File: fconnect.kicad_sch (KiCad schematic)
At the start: 198 parts, among them J1 9001-11961C00A, J2 9001-11961C00A, J3 7760, J4 7760

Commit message: First try to fit electronic on PCB
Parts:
- TP17, TP18, TP19, TP20, TP21, TP22: footprint Connector_Pin:Pin_D1.2mm_L11.3mm_W3.0mm_Flat -> Connector_Pin:Pin_D1.0mm_L10.0mm
- TP23: renamed from TP25; footprint Connector_Pin:Pin_D1.2mm_L11.3mm_W3.0mm_Flat -> Connector_Pin:Pin_D1.0mm_L10.0mm
- TP24: renamed from TP27; footprint Connector_Pin:Pin_D1.2mm_L11.3mm_W3.0mm_Flat -> Connector_Pin:Pin_D1.0mm_L10.0mm
- TP25: renamed from TP28; footprint Connector_Pin:Pin_D1.2mm_L11.3mm_W3.0mm_Flat -> Connector_Pin:Pin_D1.0mm_L10.0mm
- renumbered NT578 to NT136, NT136 to NT137, NT137 to NT138, NT138 to NT139, NT139 to NT140, NT140 to NT141, NT141 to NT142, NT142 to NT143, NT143 to NT144, NT144 to NT145, NT145 to NT146, NT146 to NT147, NT147 to NT148, NT148 to NT149, NT149 to NT150, NT150 to NT151, NT151 to NT152, NT152 to NT153, NT153 to NT154, NT154 to NT155, NT155 to NT156, NT156 to NT157, NT157 to NT158, NT158 to NT159, NT159 to NT160, NT160 to NT161, NT161 to NT162, NT162 to NT163, NT163 to NT164, NT164 to NT165, NT165 to NT166, NT579 to NT167, NT166 to NT168, NT167 to NT169, NT168 to NT170, NT169 to NT171, NT170 to NT172, NT171 to NT173, NT172 to NT174, NT173 to NT175, NT174 to NT176, NT175 to NT177, NT176 to NT178, NT177 to NT179, NT178 to NT180, NT179 to NT181, NT180 to NT182, NT181 to NT183, NT182 to NT184, NT183 to NT185, NT184 to NT186, NT185 to NT187, NT186 to NT188, NT187 to NT189, NT188 to NT190, NT189 to NT191, NT190 to NT192, NT191 to NT193, NT192 to NT194, NT193 to NT195, NT194 to NT196, NT195 to NT197, NT580 to NT198, NT196 to NT199, NT197 to NT200, NT198 to NT201, NT199 to NT202, NT200 to NT203, NT201 to NT204, NT202 to NT205, NT203 to NT206, NT204 to NT207, NT205 to NT208, NT206 to NT209, NT207 to NT210, NT208 to NT211, NT209 to NT212, NT210 to NT213, NT211 to NT214, NT212 to NT215, NT213 to NT216, NT214 to NT217, NT215 to NT218, NT216 to NT219, NT217 to NT220, NT218 to NT221, NT219 to NT222, NT220 to NT223, NT221 to NT224, NT222 to NT225, NT223 to NT226, NT224 to NT227, NT225 to NT228, NT226 to NT229, NT227 to NT230, NT228 to NT231, NT229 to NT232
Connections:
- net PM3_IO28 renamed PM2_IO28
- net PM3_IO8 renamed PM2_IO8
- net PM3_IO9 renamed PM2_IO9

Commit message: backup 1 bank done
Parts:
- NT100, NT101, NT102, NT103, NT104, NT105, NT106, NT107, NT108, NT109, NT110, NT111, NT112, NT113, NT114, NT115, NT116, NT117, NT118, NT119, NT120, NT121, NT122, NT123, NT124, NT125, NT126, NT127, NT128, NT129, NT130, NT131, NT132, NT133, NT134, NT135, NT136, NT137, NT138, NT139, NT140, NT141, NT142, NT143, NT144, NT145, NT146, NT147, NT148, NT149, NT150, NT151, NT152, NT153, NT154, NT155, NT156, NT157, NT158, NT159, NT160, NT161, NT162, NT163, NT164, NT165, NT166, NT167, NT168, NT169, NT170, NT171, NT172, NT173, NT174, NT175, NT176, NT177, NT178, NT179, NT180, NT181, NT182, NT183, NT184, NT185, NT186, NT187, NT188, NT189, NT190, NT191, NT192, NT193, NT194, NT195, NT196, NT197, NT198, NT199, NT200, NT201, NT202, NT203, NT204, NT205, NT206, NT207, NT208, NT209, NT210, NT211, NT212, NT213, NT214, NT215, NT216, NT217, NT218, NT219, NT220, NT221, NT222, NT223, NT224, NT225, NT226, NT227, NT228, NT229, NT230, NT231, NT232, NT48, NT49, NT50, NT51, NT52, NT53, NT54, NT55, NT56, NT57, NT58, NT59, NT60, NT61, NT62, NT63, NT64, NT65, NT66, NT67, NT68, NT69, NT70, NT71, NT72, NT73, NT74, NT75, NT76, NT77, NT78, NT79, NT80, NT81, NT82, NT83, NT84, NT85, NT86, NT87, NT88, NT89, NT90, NT91, NT92, NT93, NT94, NT95, NT96, NT97, NT98, NT99: footprint NetTie:NetTie-2_THT_Pad1.0mm -> NetTie:NetTie-2_Front1.0mm
- TP17, TP18, TP19, TP20, TP21, TP22, TP23, TP24, TP25: footprint Connector_Pin:Pin_D1.0mm_L10.0mm -> Connector_Pin:Pin_D0.9mm_L10.0mm_W2.4mm_FlatFork
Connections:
- net AWG_H: now also NT135.2; no longer NT135.1
- net AWG_L: now also NT139.2; no longer NT139.1
- net SCOPE_CH1_H: now also NT73.2; no longer NT73.1
- net SCOPE_CH1_L: now also NT76.2; no longer NT76.1
- net at J2.A7: now also NT73.1; no longer NT73.2
- net at J2.A24: now also NT139.1; no longer NT139.2
- net at J2.A23: now also NT135.1; no longer NT135.2
- net at J2.A8: now also NT76.1; no longer NT76.2

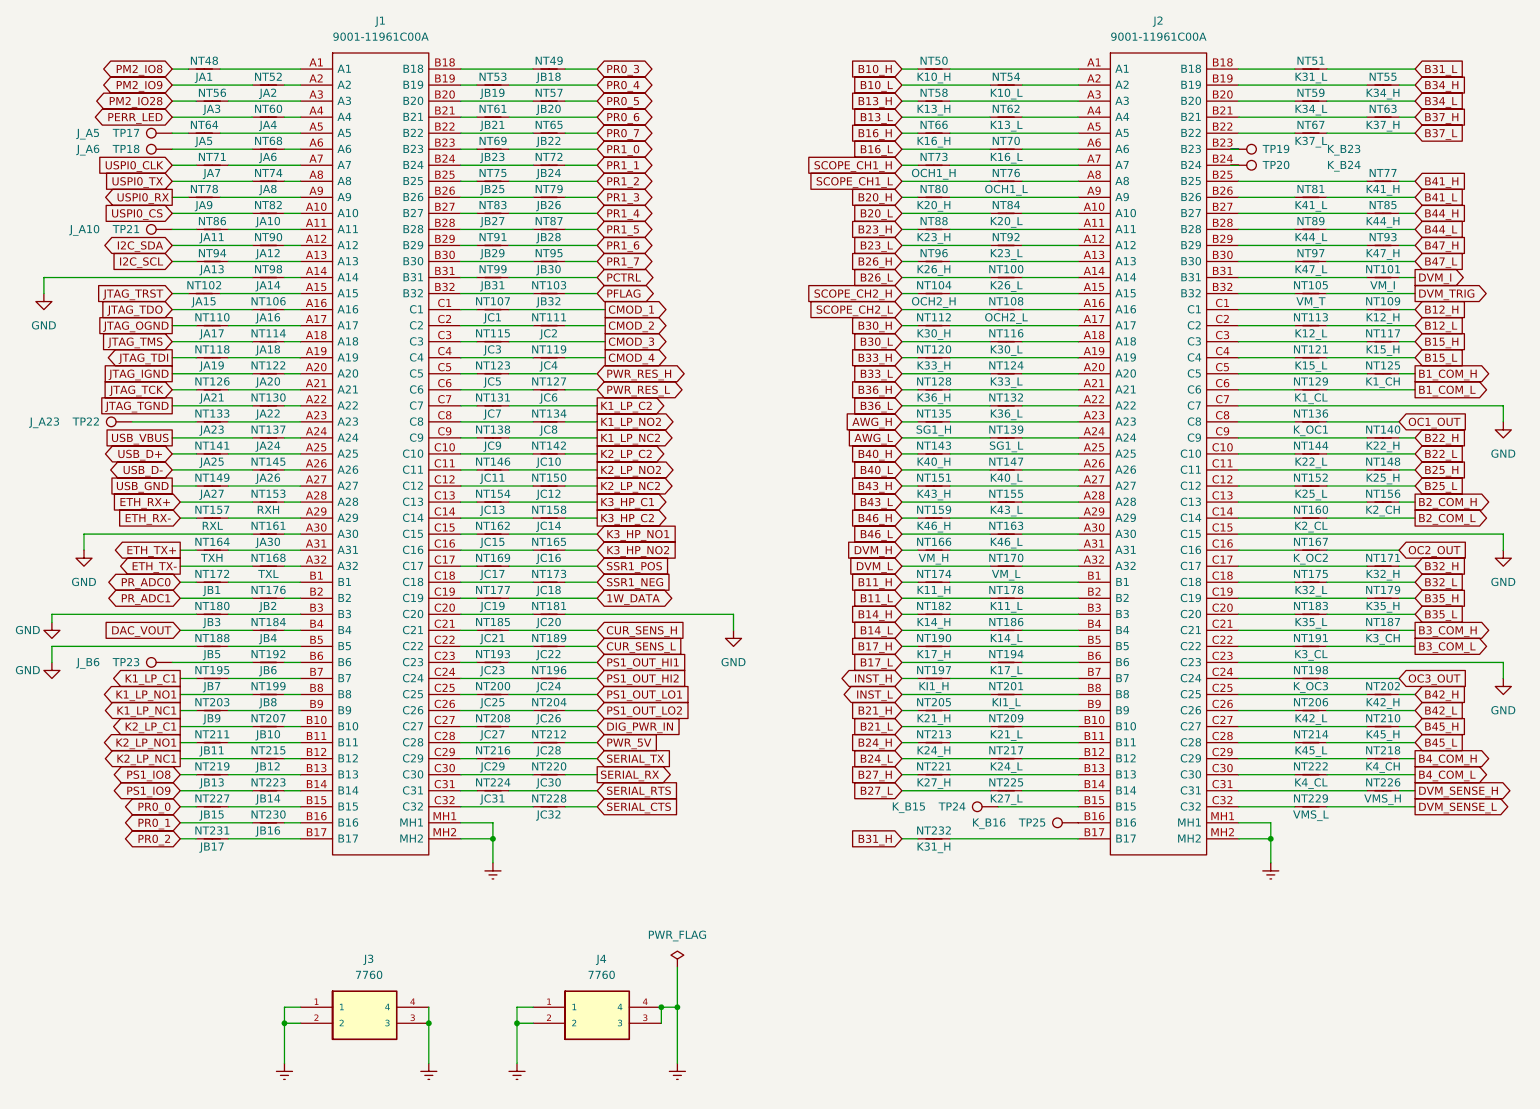
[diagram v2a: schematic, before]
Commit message: half PCB completed
FTS io controller PCB
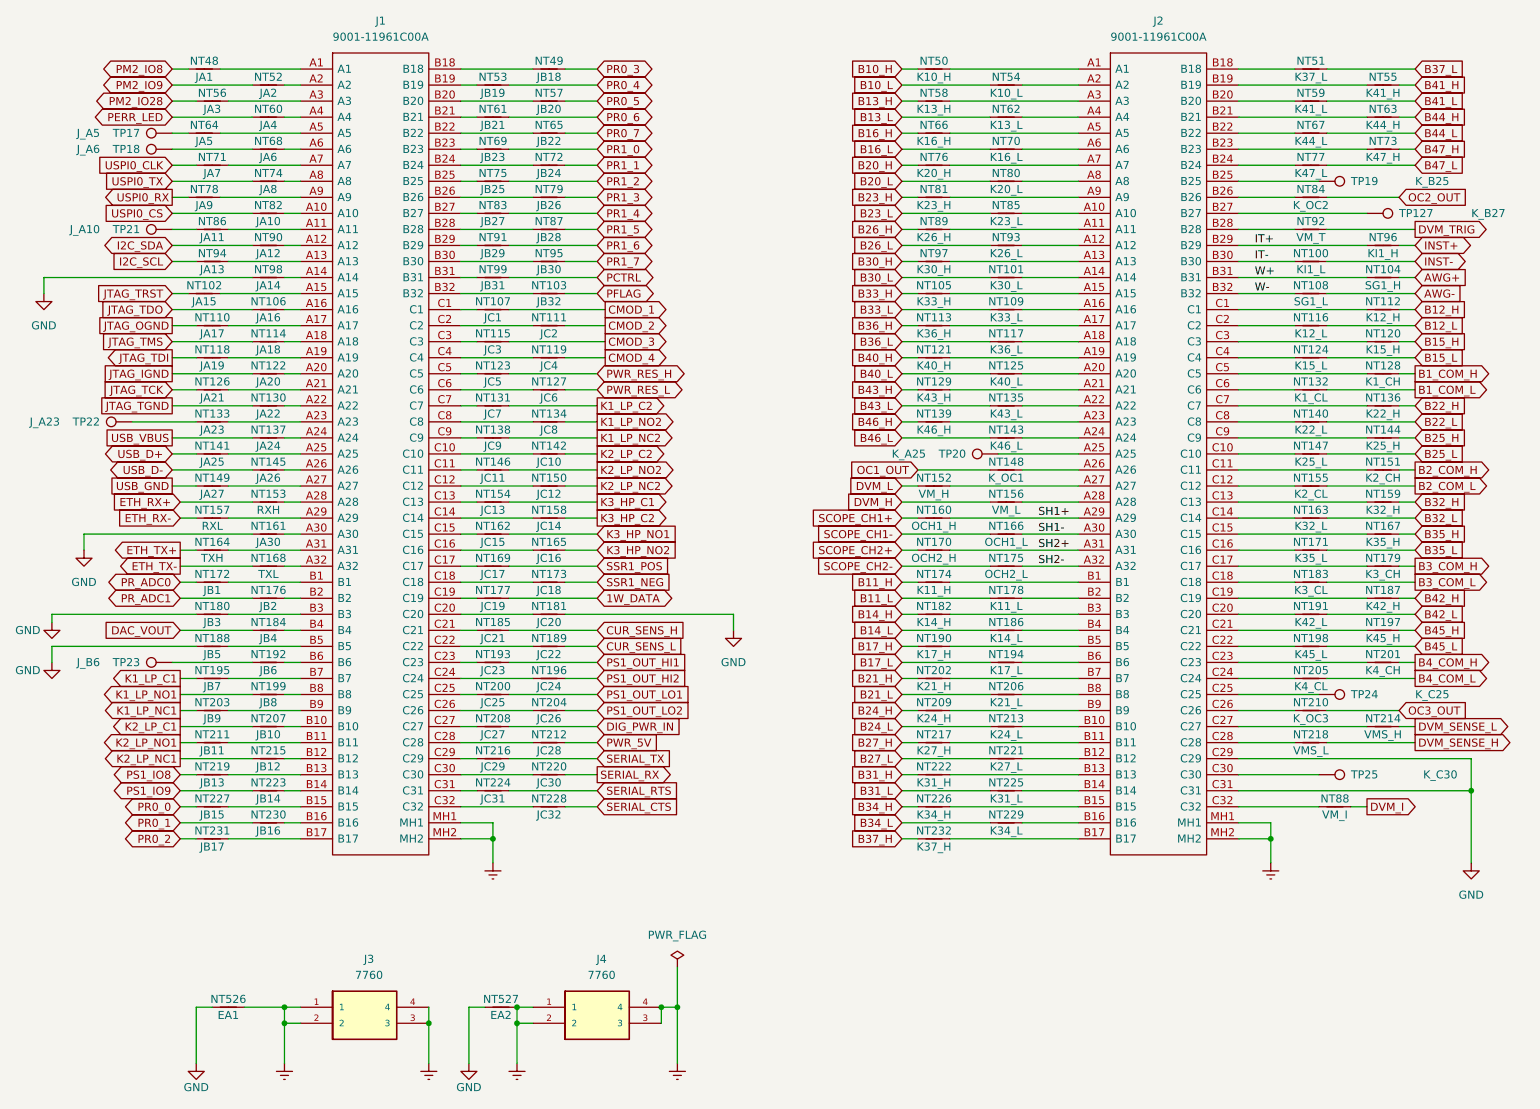
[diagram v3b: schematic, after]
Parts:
- added NT526: EA1, NetTie:NetTie-2_Front1.0mm, symbol Device:NetTie_2
- added NT527: EA2, NetTie:NetTie-2_Front1.0mm, symbol Device:NetTie_2
- added TP127: K_B27, TestPoint:TestPoint_THTPad_D1.5mm_Drill0.7mm, symbol Connector:TestPoint
- NT100: value K26_L -> KI1_L
- NT101: value VM_I -> K30_L
- NT104: value OCH2_H -> SG1_H
- NT105: value VM_T -> K33_H
- NT108: value OCH2_L -> SG1_L
- NT109: value K12_H -> K33_L
- NT112: value K30_H -> K12_H
- NT113: value K12_L -> K36_H
- NT116: value K30_L -> K12_L
- NT117: value K15_H -> K36_L
- NT120: value K33_H -> K15_H
- NT121: value K15_L -> K40_H
- NT124: value K33_L -> K15_L
- NT125: value K1_CH -> K40_L
- NT128: value K36_H -> K1_CH
- NT129: value K1_CL -> K43_H
- NT132: value K36_L -> K1_CL
- NT135: value SG1_H -> K43_L
- NT136: value K_OC1 -> K22_H
- NT139: value SG1_L -> K46_H
- NT140: value K22_H -> K22_L
- NT143: value K40_H -> K46_L
- NT144: value K22_L -> K25_H
- NT147: value K40_L -> K25_L
- NT148: value K25_H -> K_OC1
- NT151: value K43_H -> K2_CH
- NT152: value K25_L -> VM_H
- NT155: value K43_L -> K2_CL
- NT156: value K2_CH -> VM_L
- NT159: value K46_H -> K32_H
- NT160: value K2_CL -> OCH1_H
- NT163: value K46_L -> K32_L
- NT166: value VM_H -> OCH1_L
- NT167: value K_OC2 -> K35_H
- NT170: value VM_L -> OCH2_H
- NT171: value K32_H -> K35_L
- NT175: value K32_L -> OCH2_L
- NT179: value K35_H -> K3_CH
- NT183: value K35_L -> K3_CL
- NT187: value K3_CH -> K42_H
- NT191: value K3_CL -> K42_L
- NT197: value KI1_H -> K45_H
- NT198: value K_OC3 -> K45_L
- NT201: value KI1_L -> K4_CH
- NT202: value K42_H -> K21_H
- NT205: value K21_H -> K4_CL
- NT206: value K42_L -> K21_L
- NT209: value K21_L -> K24_H
- NT210: value K45_H -> K_OC3
- NT213: value K24_H -> K24_L
- NT214: value K45_L -> VMS_H
- NT217: value K24_L -> K27_H
- NT218: value K4_CH -> VMS_L
- NT221: value K27_H -> K27_L
- NT222: value K4_CL -> K31_H
- NT225: value K27_L -> K31_L
- NT226: value VMS_H -> K34_H
- NT229: value VMS_L -> K34_L
- NT232: value K31_H -> K37_H
- NT51: value K31_L -> K37_L
- NT55: value K34_H -> K41_H
- NT59: value K34_L -> K41_L
- NT63: value K37_H -> K44_H
- NT67: value K37_L -> K44_L
- NT73: value OCH1_H -> K47_H
- NT76: value OCH1_L -> K20_H
- NT77: value K41_H -> K47_L
- NT80: value K20_H -> K20_L
- NT81: value K41_L -> K23_H
- NT84: value K20_L -> K_OC2
- NT85: value K44_H -> K23_L
- NT88: value K23_H -> VM_I
- NT89: value K44_L -> K26_H
- NT92: value K23_L -> VM_T
- NT93: value K47_H -> K26_L
- NT96: value K26_H -> KI1_H
- NT97: value K47_L -> K30_H
- TP19: value K_B23 -> K_B25; footprint Connector_Pin:Pin_D0.9mm_L10.0mm_W2.4mm_FlatFork -> TestPoint:TestPoint_THTPad_D1.5mm_Drill0.7mm
- TP20: value K_B24 -> K_A25; footprint Connector_Pin:Pin_D0.9mm_L10.0mm_W2.4mm_FlatFork -> TestPoint:TestPoint_THTPad_D1.5mm_Drill0.7mm
- TP24: value K_B15 -> K_C25; footprint Connector_Pin:Pin_D0.9mm_L10.0mm_W2.4mm_FlatFork -> TestPoint:TestPoint_THTPad_D1.5mm_Drill0.7mm
- TP25: value K_B16 -> K_C30; footprint Connector_Pin:Pin_D0.9mm_L10.0mm_W2.4mm_FlatFork -> TestPoint:TestPoint_THTPad_D1.5mm_Drill0.7mm
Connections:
- net AWG_H is gone; now on net B43_L: NT135.2
- net AWG_L is gone; now on net B46_H: NT139.2
- net INST_H is gone; now on an unnamed net: NT197.1
- net INST_L is gone; now on net B4_COM_H: NT201.1
- net SCOPE_CH1_H is gone; now on net B47_H: NT73.2
- net SCOPE_CH1_L is gone; now on net B20_H: NT76.2
- net B12_H: now also NT112.2; no longer NT109.2
- net B12_L: now also NT116.2; no longer NT113.2
- net B15_H: now also NT120.2; no longer NT117.2
- net B15_L: now also NT124.2; no longer NT121.2
- net B1_COM_H: now also NT128.1; no longer NT125.1
- net B1_COM_L: now also NT132.1; no longer NT129.1
- net B20_H: no longer NT80.2
- net B20_L: now also NT80.2; no longer NT84.2
- net B21_H: now also NT202.2; no longer NT205.2
- net B21_L: now also NT206.2; no longer NT209.2
- net B22_H: now also NT136.2; no longer NT140.2
- net B22_L: now also NT140.2; no longer NT144.2
- net B23_H: now also NT81.2; no longer NT88.2
- net B23_L: now also NT85.2; no longer NT92.2
- net B24_H: now also NT209.2; no longer NT213.2
- net B24_L: now also NT213.2; no longer NT217.2
- net B25_H: now also NT144.2; no longer NT148.2
- net B25_L: now also NT147.2; no longer NT152.2
- net B26_H: now also NT89.2; no longer NT96.2
- net B26_L: now also NT93.2; no longer NT100.2
- net B27_H: now also NT217.2; no longer NT221.2
- net B27_L: now also NT221.2; no longer NT225.2
- net B2_COM_H: now also NT151.1; no longer NT156.1
- net B2_COM_L: now also NT155.1; no longer NT160.1
- net B30_H: now also NT97.2; no longer NT112.2
- net B30_L: now also NT101.2; no longer NT116.2
- net B31_H: now also NT222.2; no longer NT232.2
- net B31_L: now also NT225.2; no longer NT51.2
- net B32_H: now also NT159.2; no longer NT171.2
- net B32_L: now also NT163.2; no longer NT175.2
- net B33_H: now also NT105.2; no longer NT120.2
- net B33_L: now also NT109.2; no longer NT124.2
- net B34_H: now also NT226.2; no longer NT55.2
- net B34_L: now also NT229.2; no longer NT59.2
- net B35_H: now also NT167.2; no longer NT179.2
- net B35_L: now also NT171.2; no longer NT183.2
- net B36_H: now also NT113.2; no longer NT128.2
- net B36_L: now also NT117.2; no longer NT132.2
- net B37_H: now also NT232.2; no longer NT63.2
- net B37_L: now also NT51.2; no longer NT67.2
- net B3_COM_H: now also NT179.2; no longer NT187.1
- net B3_COM_L: now also NT183.2; no longer NT191.1
- net B40_H: now also NT121.2; no longer NT143.2
- net B40_L: now also NT125.2; no longer NT147.2
- net B41_H: now also NT55.2; no longer NT77.2
- net B41_L: now also NT59.2; no longer NT81.2
- net B42_H: now also NT187.1; no longer NT202.2
- net B42_L: now also NT191.2; no longer NT206.2
- net B43_H: now also NT129.2; no longer NT151.2
- net B43_L: no longer NT155.2
- net B44_H: now also NT63.2; no longer NT85.2
- net B44_L: now also NT67.2; no longer NT89.2
- net B45_H: now also NT197.2; no longer NT210.2
- net B45_L: now also NT198.2; no longer NT214.2
- net B46_H: no longer NT159.2
- net B46_L: now also NT143.2; no longer NT163.2
- net B47_H: no longer NT93.2
- net B47_L: now also NT77.2; no longer NT97.2
- net B4_COM_H: no longer NT218.1
- net B4_COM_L: now also NT205.1; no longer NT222.1
- net DVM_H: now also NT156.2; no longer NT166.2
- net DVM_I: now also NT88.2; no longer NT101.2
- net DVM_L: now also NT152.2; no longer NT170.2
- net DVM_SENSE_H: now also NT218.2; no longer NT226.2
- net DVM_SENSE_L: now also NT214.2; no longer NT229.2
- net DVM_TRIG: now also NT92.2; no longer NT105.2
- net Earth: now also NT526.1, NT527.1
- net GND: now also J2.C29, J2.C31, NT526.2, NT527.2; no longer J2.C15, J2.C23, J2.C7
- net OC1_OUT: now also NT148.1; no longer NT136.1
- net OC2_OUT: now also NT84.1; no longer NT167.1
- net OC3_OUT: now also NT210.1; no longer NT198.1
- net at J2.B12: now also NT221.1; no longer NT217.1
- net at NT88.1: now also J2.C32; no longer J2.A11
- net at NT117.1: now also J2.A18; no longer J2.C3
- net at TP25.1: now also J2.C30; no longer J2.B16
- net at NT226.1: now also J2.B15; no longer J2.C31
- net at J2.B11: now also NT217.1; no longer NT213.1
- net SCOPE_CH2+: now reaches NT170.1
- net SCOPE_CH2+: no longer J2.A32
- net at J2.A26: now also NT148.2; no longer NT147.1
- net at NT89.1: now also J2.A11; no longer J2.B28
- net at J2.A13: now also NT97.1; no longer NT96.1
- net at J2.B7: now also NT202.1; no longer NT197.2
- net at J2.C16: now also NT171.1; no longer NT167.2
- net at J2.C5: now also NT128.2; no longer NT125.2
- net at J2.A7: now also NT76.1; no longer NT73.1
- net at NT112.1: now also J2.C1; no longer J2.A17
- net at TP19.1: now also J2.B25; no longer J2.B23
- net at NT179.1: now also J2.C17; no longer J2.C19
- net IT-: now reaches J2.B30
- net IT-: now also NT100.2; no longer NT97.1
- net at NT159.1: now also J2.C13; no longer J2.A29
- net at J2.B27: now also TP127.1; no longer NT85.1
- net at NT109.1: now also J2.A16; no longer J2.C1
- net at J2.A28: now also NT156.1; no longer NT155.1
- net at J2.A22: now also NT135.1; no longer NT132.1
- net at J2.C21: no longer NT187.2
- net at J2.A10: now also NT85.1; no longer NT84.1
- net at TP24.1: now also J2.C25; no longer J2.B15
- net at J2.C26: now also NT210.2; no longer NT206.1
- net at J2.C20: now also NT191.1; no longer NT183.1
- net at J2.B24: now also NT77.1; no longer TP20.1
- net at NT93.1: now also J2.A12; no longer J2.B29
- net at J2.C2: now also NT116.1; no longer NT113.1
- net at J2.C4: now also NT124.1; no longer NT121.1
- net at J2.A19: now also NT121.1; no longer NT120.1
- net at J2.C22: now also NT198.1; no longer NT191.2
- net at J2.A24: now also NT143.1; no longer NT139.1
- net at NT214.1: now also J2.C27; no longer J2.C28
- net at J2.C18: now also NT183.1; no longer NT175.1
- net at J2.C10: now also NT147.1; no longer NT144.1
- net at NT163.1: now also J2.C14; no longer J2.A30
- net at NT101.1: now also J2.A14; no longer J2.B31
- net SCOPE_CH1+: now reaches NT160.2
- net SCOPE_CH1+: no longer J2.C14
- net at J2.A23: now also NT139.1; no longer NT135.1
- net at J2.B8: now also NT206.1; no longer NT201.2
- net AWG-: now reaches NT108.2
- net AWG-: no longer J2.A16
- net at J2.C6: now also NT132.2; no longer NT129.2
- net at NT80.1: now also J2.A8; no longer J2.A9
- net at J2.C8: now also NT140.1; no longer NT136.2
- net at J2.B13: now also NT222.1; no longer NT221.1
- net at J2.A25: now also TP20.1; no longer NT143.1
- net at NT105.1: now also J2.A15; no longer J2.B32
- net at J2.C12: now also NT155.2; no longer NT152.1
- net at NT81.1: now also J2.A9; no longer J2.B26
- net INST-: now reaches NT100.1
- net INST-: no longer J2.A14
- net at J2.B9: now also NT209.1; no longer NT205.1
- net at J2.A20: now also NT125.1; no longer NT124.1
- net at NT92.1: now also J2.B28; no longer J2.A12
- net at J2.A27: now also NT152.1; no longer NT151.1
- net at J2.C11: now also NT151.2; no longer NT148.1
- net SH1-: now reaches NT166.1
- net SH1-: now also J2.A30; no longer J2.A31
- net AWG+: now reaches NT104.2
- net AWG+: no longer J2.A15
- net at J2.A21: now also NT129.1; no longer NT128.1
- net at J2.B10: now also NT213.1; no longer NT209.1
- net at J2.C24: now also NT205.2; no longer NT198.2
- net at NT229.1: now also J2.B16; no longer J2.C32
- net at J2.C9: now also NT144.1; no longer NT140.1
- net SCOPE_CH2_H renamed W+
- net W+: now also J2.B31
- net SCOPE_CH2_L renamed W-
- net W-: now also J2.B32
- new net: J2.B23, NT73.1
- new net: J2.B26, NT84.2
- new net: J2.C15, NT167.1
- new net: J2.A17, NT113.1
- new net: J2.C19, NT187.2
- new net: J2.C23, NT201.2
- new net: J2.C28, NT218.1
- new net: J2.C3, NT120.1
- new net: J2.C7, NT136.1
- new net INST+: NT96.1
- new net IT+: J2.B29, NT96.2
- new net SCOPE_CH1-: NT166.2
- new net SCOPE_CH2-: NT175.1
- new net SH1+: J2.A29, NT160.1
- new net SH2+: J2.A31, NT170.2
- new net SH2-: J2.A32, NT175.2
